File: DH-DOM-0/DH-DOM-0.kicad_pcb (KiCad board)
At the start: 2 copper layers, 40 x 40 mm, 36 parts, among them J1 USB_C_Receptacle_USB2.0_14P, SW1 RST, SW2 BOOT, U1 MMC5983MA, U2 BMI270, U3 ESP32-S3-WROOM-1, U4 NCP1117-3.3_SOT223, U5 TVS1400DRV, U6 SSD1306

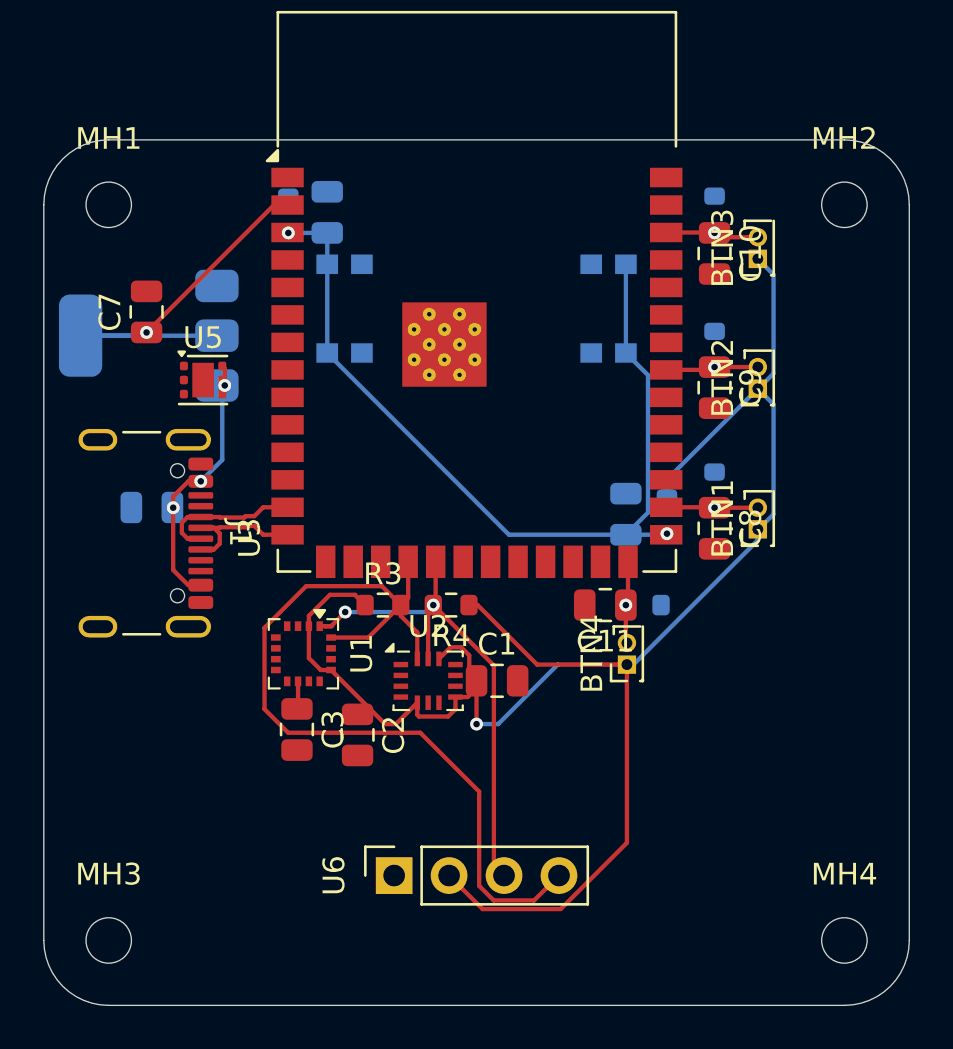
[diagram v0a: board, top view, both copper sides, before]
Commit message: fix
+ no more relevant DRC errors
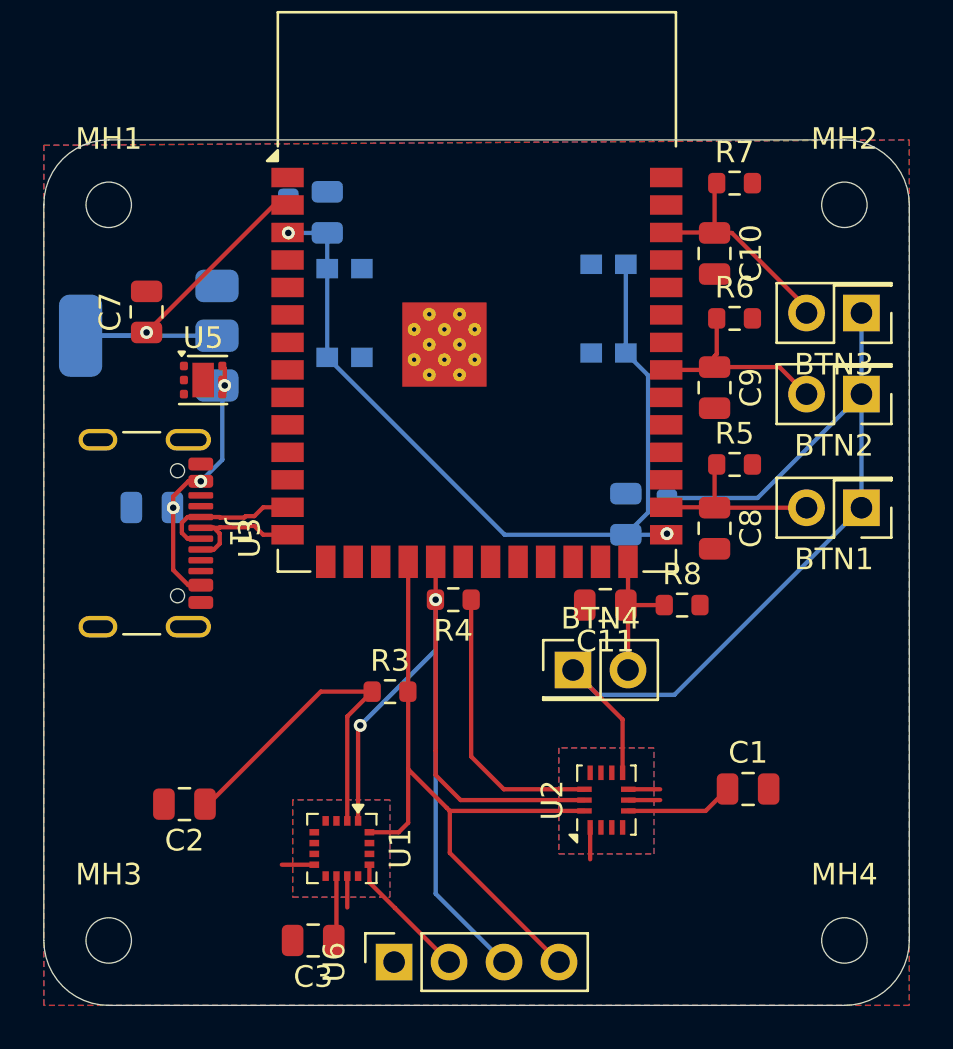
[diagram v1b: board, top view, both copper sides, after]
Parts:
- BTN1, BTN2, BTN3, BTN4: footprint Connector_PinHeader_1.00mm:PinHeader_2x01_P1.00mm_Vertical -> Connector_PinHeader_2.54mm:PinHeader_2x01_P2.54mm_Vertical
- R5, R6, R7, R8: moved to F.Cu
- moved C1 12.6 mm to (203.1, 115.5)
- moved U2 9.91 mm to (196.5, 116.0), turned to 90 degrees
- moved C3 9.78 mm to (182.9, 122.5), turned to 180 degrees
- moved U1 9.17 mm to (184.3, 118.2)
- moved C2 8.62 mm to (177.0, 116.2), turned to 180 degrees
- moved BTN3 5.40 mm to (208.3, 93.5), turned to 180 degrees
- moved BTN1 4.89 mm to (208.3, 102.5), turned to 180 degrees
- moved BTN2 4.80 mm to (208.3, 97.2), turned to 180 degrees
- moved R3 4.01 mm to (186.5, 111.0)
- moved U6 4.00 mm to (186.7, 123.5)
- moved BTN4 2.50 mm to (195.0, 110.0), turned to 0 degrees
- moved R8 1.80 mm to (200.0, 107.0)
- moved R6 1.70 mm to (202.4, 93.8), turned to 0 degrees
- moved R7 1.70 mm to (202.4, 87.5), turned to 0 degrees
- moved R5 1.50 mm to (202.4, 100.5), turned to 0 degrees
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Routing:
- net /SCL: track 25.0 -> 44.7 mm
- net /SDA: track 40.3 -> 32.1 mm
- net GND: track 0.00 -> 7.38 mm
- net /BTN3: track 4.33 -> 10.9 mm, vias 1 -> 0
- net /BTN2: track 4.29 -> 9.35 mm, vias 1 -> 0
- net /BTN1: track 4.24 -> 8.53 mm, vias 1 -> 0
- net /BTN4: track 3.81 -> 7.37 mm, vias 1 -> 0
- net +3V3: track 103.9 -> 101.9 mm, vias 2 -> 1
- net Net-(U1-CAP): track 1.30 -> 3.03 mm
- added copper zone on B.Cu, net GND
- added copper zone on F.Cu, net GND

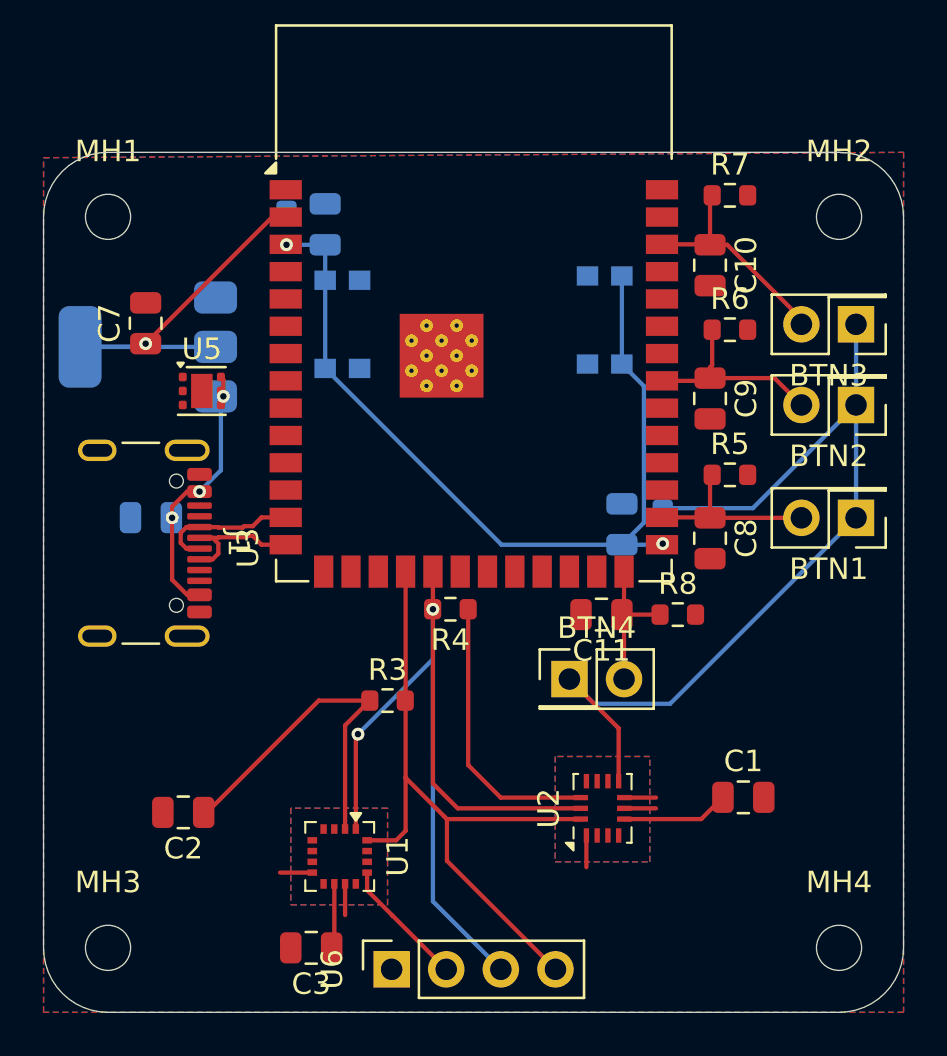
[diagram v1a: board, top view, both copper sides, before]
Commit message: fix
+ fixed ground plane
- excluded DRC errors for through hole clearance violation for ESP32 gnd pad and USB pins
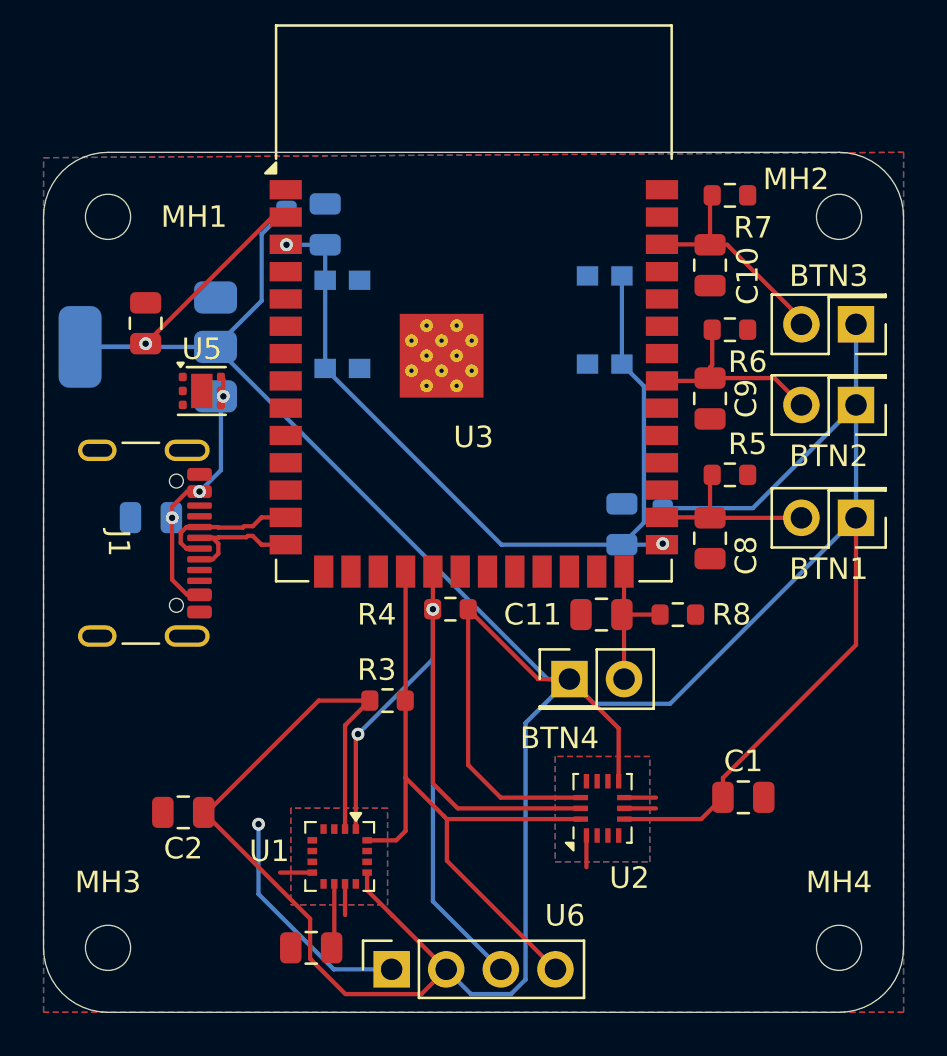
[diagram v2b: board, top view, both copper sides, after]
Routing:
- net +3V3: track 101.9 -> 189.8 mm
- net GND: track 7.38 -> 18.3 mm, vias 0 -> 1
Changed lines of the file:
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@@
 		(tags "capacitor")
 		(property "Reference" "C10"
-			(at 0 -1.68 90)
+			(at 0.5 -1.75 90)
 			(layer "F.SilkS")
 			(effects
@@
 		(tags "lga land grid array")
 		(property "Reference" "U2"
-			(at 0 -2.5 90)
+			(at -3.2375 1.25 180)
 			(layer "F.SilkS")
 			(effects
@@
 		(tags "mountinghole")
 		(property "Reference" "MH2"
-			(at 0 -3.05 0)
+			(at -2 -1.75 0)
 			(layer "F.SilkS")
 			(effects
@@
 			(at 0 1.95 0)
 			(layer "F.Fab")
+			(hide yes)
 			(effects
 				(font
@@
 		(tags "lga land grid array")
 		(property "Reference" "U1"
-			(at 0 -2.7 90)
+			(at -0.25 3.275 0)
 			(layer "F.SilkS")
 			(effects
@@
 			(at 0 2.75 90)
 			(layer "F.Fab")
+			(hide yes)
 			(effects
 				(font
@@
 		(tags "capacitor")
 		(property "Reference" "C11"
-			(at 0 -1.68 0)
+			(at 3.2 0 0)
 			(layer "F.SilkS")
 			(effects
@@
 			(at 0 -1.68 90)
 			(layer "F.SilkS")
+			(hide yes)
 			(effects
 				(font
@@
 		)
 		(property "Value" "10u"
-			(at 0 1.68 90)
+			(at -0.05 -1.75 90)
 			(layer "F.Fab")
 			(effects
@@
 		(tags "USB C Type-C Receptacle SMD USB 2.0 16P 16C USB4105-15-A USB4105-15-A-060 USB4105-15-A-120 USB4105-GF-A USB4105-GF-A-060 USB4105-GF-A-120")
 		(property "Reference" "J1"
-			(at 0 -5.5 270)
+			(at 0 0.075 270)
 			(unlocked yes)
 			(layer "F.SilkS")
@@
 			(unlocked yes)
 			(layer "F.Fab")
+			(hide yes)
 			(effects
 				(font
@@
 		(tags "resistor")
 		(property "Reference" "R3"
-			(at 0 -1.43 0)
+			(at -0.5 -1.43 0)
 			(layer "F.SilkS")
 			(effects
@@
 		(tags "resistor")
 		(property "Reference" "R5"
-			(at 0 -1.43 0)
+			(at 0.825 -1.43 180)
 			(layer "F.SilkS")
 			(effects
@@
 		(tags "resistor")
 		(property "Reference" "R7"
-			(at 0 -1.43 0)
+			(at 1.075 1.5 0)
 			(layer "F.SilkS")
 			(effects
@@
 		(tags "capacitor")
 		(property "Reference" "C8"
-			(at 0 -1.68 90)
+			(at 0.8 -1.68 90)
 			(layer "F.SilkS")
 			(effects
@@
 		(tags "mountinghole")
 		(property "Reference" "MH1"
-			(at 0 -3.05 0)
+			(at 4 0 0)
 			(layer "F.SilkS")
 			(effects
@@
 			(at 0 3.05 0)
 			(layer "F.Fab")
+			(hide yes)
 			(effects
 				(font
@@
 		(tags "resistor")
 		(property "Reference" "R6"
-			(at 0 -1.43 0)
+			(at 0.825 1.5 0)
 			(layer "F.SilkS")
 			(effects
@@
 		(tags "resistor")
 		(property "Reference" "R4"
-			(at 0 -1.43 0)
+			(at 3.425 -0.25 0)
 			(layer "F.SilkS")
 			(effects
@@
 		(tags "2.4 GHz Wi-Fi and Bluetooth module")
 		(property "Reference" "U3"
-			(at -10.5 11.4 90)
+			(at -0.015 6.25 0)
 			(unlocked yes)
 			(layer "F.SilkS")
@@
 		(tags "Through hole pin header THT 2x01 2.54mm double row")
 		(property "Reference" "BTN4"
-			(at 1.27 -2.38 0)
+			(at -0.46 2.75 0)
 			(layer "F.SilkS")
 			(effects
@@
 		(tags "Through hole pin header THT 2x01 2.54mm double row")
 		(property "Reference" "BTN3"
-			(at 1.27 -2.38 0)
+			(at 1.27 2.25 0)
 			(layer "F.SilkS")
 			(effects
@@
 		(tags "capacitor")
 		(property "Reference" "C3"
-			(at 0 -1.68 0)
+			(at 2.45 0 0)
 			(layer "F.SilkS")
+			(hide yes)
 			(effects
 				(font
@@
 		)
 		(property "Value" "10u"
-			(at 0 1.68 0)
+			(at 0.7 -1.75 0)
 			(layer "F.Fab")
 			(effects
@@
 		(tags "Through hole socket strip THT 1x04 2.54mm single row")
 		(property "Reference" "U6"
-			(at 0 -2.77 90)
+			(at 2.5 8.06 180)
 			(layer "F.SilkS")
 			(effects
@@
 		(tags "resistor")
 		(property "Reference" "R8"
-			(at 0 -1.43 0)
+			(at 2.5 0 0)
 			(layer "F.SilkS")
 			(effects
@@
 			(at 0 -4.5 0)
 			(layer "B.Fab")
+			(hide yes)
 			(effects
 				(font
@@
 		(net "GND")
 	)
+	(via
+		(at 180.5 116.75)
+		(size 0.6)
+		(drill 0.3)
+		(layers "F.Cu" "B.Cu")
+		(net "GND")
+	)
+	(segment
+		(start 180.5 120)
+		(end 180.5 116.75)
+		(width 0.2)
+		(layer "B.Cu")
+		(net "GND")
+	)
+	(segment
+		(start 186.69 123.5)
+		(end 184 123.5)
+		(width 0.2)
+		(layer "B.Cu")
+		(net "GND")
+	)
+	(segment
+		(start 184 123.5)
+		(end 180.5 120)
+		(width 0.2)
+		(layer "B.Cu")
+		(net "GND")
+	)
 	(segment
 		(start 201.5 87.6)
@@
 	)
 	(segment
+		(start 202.1 115.5)
+		(end 202.1 114.6)
+		(width 0.2)
+		(layer "F.Cu")
+		(net "+3V3")
+	)
+	(segment
 		(start 201.0875 116.5125)
 		(end 197.5125 116.5125)
@@
 	)
 	(segment
+		(start 194.96 110)
+		(end 193.5 110)
+		(width 0.2)
+		(layer "F.Cu")
+		(net "+3V3")
+	)
+	(segment
 		(start 190.25 114)
 		(end 191.7625 115.5125)
@@
 	)
 	(segment
+		(start 184.540256 124.65)
+		(end 188.08 124.65)
+		(width 0.2)
+		(layer "F.Cu")
+		(net "+3V3")
+	)
+	(segment
 		(start 186.73 121)
 		(end 189.23 123.5)
@@
 	)
 	(segment
+		(start 177.95 116.2)
+		(end 182.9 121.15)
+		(width 0.2)
+		(layer "F.Cu")
+		(net "+3V3")
+	)
+	(segment
 		(start 185.675 111)
 		(end 183.3 111)
@@
 	)
 	(segment
+		(start 182.9 121.15)
+		(end 182.9 123.009744)
+		(width 0.2)
+		(layer "F.Cu")
+		(net "+3V3")
+	)
+	(segment
+		(start 182.9 123.009744)
+		(end 184.540256 124.65)
+		(width 0.2)
+		(layer "F.Cu")
+		(net "+3V3")
+	)
+	(segment
 		(start 181.14 88.51)
 		(end 181.765 88.51)
@@
 	)
 	(segment
+		(start 188.08 124.65)
+		(end 189.23 123.5)
+		(width 0.2)
+		(layer "F.Cu")
+		(net "+3V3")
+	)
+	(segment
 		(start 191.7625 115.5125)
 		(end 195.4875 115.5125)
@@
 		(net "+3V3")
 	)
+	(segment
+		(start 208.29 108.41)
+		(end 208.29 102.5)
+		(width 0.2)
+		(layer "F.Cu")
+		(net "+3V3")
+	)
+	(segment
+		(start 202.1 114.6)
+		(end 208.29 108.41)
+		(width 0.2)
+		(layer "F.Cu")
+		(net "+3V3")
+	)
+	(segment
+		(start 193.5 110)
+		(end 190.25 106.75)
+		(width 0.2)
+		(layer "F.Cu")
+		(net "+3V3")
+	)
 	(via
 		(at 175.25 94.4)
@@
 	)
 	(segment
+		(start 194.96 110)
+		(end 193.95 110)
+		(width 0.2)
+		(layer "B.Cu")
+		(net "+3V3")
+	)
+	(segment
 		(start 199.3 102.05)
 		(end 203.49 102.05)
@@
 	)
 	(segment
+		(start 190.38 124.65)
+		(end 189.23 123.5)
+		(width 0.2)
+		(layer "B.Cu")
+		(net "+3V3")
+	)
+	(segment
+		(start 181.8 88.15)
+		(end 180.645406 89.304594)
+		(width 0.2)
+		(layer "B.Cu")
+		(net "+3V3")
+	)
+	(segment
 		(start 175.1 94.55)
 		(end 175.25 94.4)
@@
 	)
 	(segment
+		(start 180.645406 89.304594)
+		(end 180.645406 92.404594)
+		(width 0.2)
+		(layer "B.Cu")
+		(net "+3V3")
+	)
+	(segment
 		(start 208.29 93.5)
 		(end 208.29 102.5)
@@
 	)
 	(segment
+		(start 194.96 110)
+		(end 192.92 112.04)
+		(width 0.2)
+		(layer "B.Cu")
+		(net "+3V3")
+	)
+	(segment
+		(start 192.92 123.976346)
+		(end 192.246346 124.65)
+		(width 0.2)
+		(layer "B.Cu")
+		(net "+3V3")
+	)
+	(segment
+		(start 192.246346 124.65)
+		(end 190.38 124.65)
+		(width 0.2)
+		(layer "B.Cu")
+		(net "+3V3")
+	)
+	(segment
+		(start 192.92 112.04)
+		(end 192.92 123.976346)
+		(width 0.2)
+		(layer "B.Cu")
+		(net "+3V3")
+	)
+	(segment
+		(start 193.95 110)
+		(end 178.5 94.55)
+		(width 0.2)
+		(layer "B.Cu")
+		(net "+3V3")
+	)
+	(segment
 		(start 208.29 102.5)
 		(end 199.64 111.15)
 		(width 0.2)
 		(layer "B.Cu")
+		(net "+3V3")
+	)
+	(segment
+		(start 180.645406 92.404594)
+		(end 178.5 94.55)
+		(width 0.2)
+		(layer "B.Cu")

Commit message: added bom
new bom
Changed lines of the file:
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@@
 			(at 0 3.05 0)
 			(layer "F.Fab")
+			(hide yes)
 			(effects
 				(font
@@
 		(tags "capacitor")
 		(property "Reference" "C1"
-			(at 0 -1.68 0)
+			(at 2.7 0 0)
 			(layer "F.SilkS")
 			(effects
@@
 			(at 0 3.05 0)
 			(layer "F.Fab")
+			(hide yes)
 			(effects
 				(font
@@
 			(at 0 3.05 0)
 			(layer "F.Fab")
+			(hide yes)
 			(effects
 				(font
@@
 		(tags "resistor")
 		(property "Reference" "R2"
-			(at 0 1.43 90)
+			(at -2.625 -0.2 90)
 			(layer "B.SilkS")
 			(effects
@@
 		)
 		(property "Value" "1K"
-			(at 0 -1.43 90)
+			(at -2.625 -1.7 90)
 			(layer "B.Fab")
 			(effects
@@
 		(tags "resistor")
 		(property "Reference" "R1"
-			(at 0 1.43 90)
+			(at 0 2.3 90)
 			(layer "B.SilkS")
 			(effects
@@
 		)
 		(property "Value" "100n"
-			(at 0 -1.68 90)
+			(at 0 3.15 90)
 			(layer "B.Fab")
 			(effects
@@
 		(tags "capacitor")
 		(property "Reference" "C6"
-			(at 0 1.68 0)
+			(at -0.005597 -1.759142 0)
 			(layer "B.SilkS")
 			(effects
@@
 		)
 		(property "Value" "10u"
-			(at 0 -1.68 0)
+			(at -3.005597 -0.009142 0)
 			(layer "B.Fab")
 			(effects
@@
 		(tags "capacitor")
 		(property "Reference" "C4"
-			(at 0 1.68 90)
+			(at 0.558608 -1.360544 90)
 			(layer "B.SilkS")
 			(effects

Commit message: edit
new imu, new footprint, edited schematic, new pcb, old one saved as I2C
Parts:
- removed R3, R4: 2.7K, Resistor_SMD:R_0603_1608Metric
- removed U6: SSD1306, Connector_PinSocket_2.54mm:PinSocket_1x04_P2.54mm_Vertical
- added U7: ST7789, Connector_PinSocket_2.54mm:PinSocket_1x08_P2.54mm_Vertical, F.Cu at (181.6, 123.5)
- C4, C6, SW1, SW2: moved to F.Cu
- R5, R6, R7, R8: moved to B.Cu
- U2: value BMI270 -> LSM6DSOXTR; footprint Package_LGA:Bosch_LGA-14_3x2.5mm_P0.5mm -> Package_LGA:LGA-14_3x2.5mm_P0.5mm_LayoutBorder3x4y
- moved C1 70.4 mm to (138.0, 88.6)
- moved U5 59.3 mm to (120.8, 112.9)
- moved C3 52.9 mm to (138.0, 94.6), turned to 0 degrees
- moved C2 46.1 mm to (138.0, 91.6), turned to 0 degrees
- moved C6 37.5 mm to (138.0, 103.7), turned to 0 degrees
- moved C7 33.1 mm to (142.5, 88.6), turned to 0 degrees
- moved C5 32.8 mm to (207.5, 111.2), turned to 0 degrees
- moved SW2 25.4 mm to (207.6, 116.2)
- moved C4 23.8 mm to (177.2, 90.2), turned to -90 degrees
- moved BTN4 23.7 mm to (202.2, 87.5), turned to -90 degrees
- moved C11 15.2 mm to (202.2, 93.0), turned to 0 degrees
- moved R8 14.0 mm to (200.4, 93.0), turned to 180 degrees
- moved R2 13.0 mm to (207.5, 113.0), turned to 180 degrees
- moved U2 10.8 mm to (185.7, 115.5), turned to 0 degrees
- moved SW1 10.6 mm to (173.8, 94.3)
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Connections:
- C5 pad 1: Net-(U3-EN) -> Net-(U3-IO0)
- R2 pad 2: Net-(U3-EN) -> Net-(U3-IO0)
- SW2 pad 2: Net-(U3-EN) -> Net-(U3-IO0)
- U1 pad 1: /SCL -> /SCLK_MAG
- U1 pad 16: /SDA -> /MOSI_MAG
- U1 pad 4: unconnected-(U1-CS-Pad4) -> /SS_MAG
- U1 pad 5: unconnected-(U1-SDO-Pad5) -> /MISO_MAG
- U2 pad 1: GND -> /MOSI_IMU
- U2 pad 12: +3V3 -> /SS_IMU
- U2 pad 13: /SCL -> /SCLK_IMU
- U2 pad 14: /SDA -> /MISO_IMU
- U3 pad 15: unconnected-(U3-IO3-Pad15) -> /MOSI_IMU
- U3 pad 16: unconnected-(U3-IO46-Pad16) -> /MISO_IMU
- U3 pad 17: unconnected-(U3-IO9-Pad17) -> /SCLK_IMU
- U3 pad 18: /SDA -> /SS_IMU
- U3 pad 19: /SCL -> /MISO_MAG
- U3 pad 20: unconnected-(U3-IO12-Pad20) -> /SS_MAG
- U3 pad 21: unconnected-(U3-IO13-Pad21) -> /SCLK_MAG
- U3 pad 22: unconnected-(U3-IO14-Pad22) -> /MOSI_MAG
- U3 pad 26: /BTN4 -> unconnected-(U3-IO45-Pad26)
- U3 pad 27: Net-(U3-EN) -> Net-(U3-IO0)
- U3 pad 28: /BTN1 -> unconnected-(U3-IO35-Pad28)
- U3 pad 32: unconnected-(U3-IO39-Pad32) -> /BTN1
- U3 pad 34: unconnected-(U3-IO41-Pad34) -> /BTN3
- U3 pad 35: unconnected-(U3-IO42-Pad35) -> /BTN4
- U3 pad 38: /BTN3 -> unconnected-(U3-IO2-Pad38)
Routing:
- net +3V3: track 189.8 -> 96.0 mm, vias 1 -> 2
- net /SCL: track 44.7 -> 0.00 mm, vias 2 -> 0
- net /SDA: track 32.1 -> 0.00 mm
- net Net-(U3-EN): track 39.8 -> 13.2 mm, vias 2 -> 1
- net Net-(U3-IO0): track 0.00 -> 18.1 mm, vias 0 -> 2
- net GND: track 18.3 -> 3.21 mm, vias 1 -> 0
- net /MOSI_IMU: track 0.00 -> 10.6 mm
- net /SS_IMU: track 0.00 -> 10.5 mm
- net /MISO_IMU: track 0.00 -> 10.2 mm
- net /SCLK_IMU: track 0.00 -> 10.2 mm
- net /MOSI_MAG: track 0.00 -> 6.53 mm
- net /MISO_MAG: track 0.00 -> 6.53 mm
- net /SS_MAG: track 0.00 -> 5.79 mm
- net /SCLK_MAG: track 0.00 -> 5.79 mm
- net /BTN3: track 10.9 -> 6.97 mm, vias 0 -> 1
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- removed copper zone on B.Cu, net GND
